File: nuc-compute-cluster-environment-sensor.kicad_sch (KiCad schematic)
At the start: 122 parts, among them J1 USB4105-GF-A, J2 SM04B-SRSS-TB-LF-SN, J3 SM04B-SRSS-TB-LF-SN, U1 FT4232H-56Q, U2 AP7370-33SA-7, U3 STM32G474CET6, U4 MB85RC1MTPNF-G, U5 SHT45, U6 BME280, Y1 ABM3B-12.000MHZ-B2-T, Y2 ECS-_327-12_5-34B-TR, Y3 ABM3B-8.000MHZ-10-1-U-T

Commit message: Reannotate schematic symbols
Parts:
- gave numbers to parts that had none: 1
- renumbered C1 to C51, C2 to C52, C3 to C53, C4 to C54, C5 to C55, C6 to C56, C7 to C57, C8 to C58, C9 to C59, C10 to C60, C11 to C61, C12 to C62, C13 to C63, C14 to C64, C15 to C65, C16 to C66, C17 to C67, C18 to C68, C19 to C69, C20 to C70, C21 to C71, C22 to C72, C23 to C73, C24 to C74, C25 to C75, C26 to C76, C27 to C77, C28 to C78, C29 to C79, C30 to C80, C31 to C81, C32 to C82, C33 to C83, C34 to C84, C35 to C85, C36 to C86, C37 to C87, C38 to C88, C39 to C89, C40 to C90, D1 to D35, D2 to D36, D3 to D37, D4 to D38, D5 to D39, D6 to D40, D7 to D41, D8 to D42, D9 to D43, FB1 to FB13, FB2 to FB14, FB3 to FB15, FB4 to FB16, FB5 to FB17, J1 to J15, J2 to J16, J3 to J17, MP1 to MP17, MP2 to MP18, MP3 to MP19, R1 to R207, R2 to R208, R3 to R209, R4 to R210, R5 to R211, R6 to R212, R7 to R213, R8 to R214, R9 to R215, R10 to R216, R11 to R217, R12 to R218, R13 to R219, R14 to R220, R15 to R221, R16 to R222, R17 to R223, R18 to R224, R19 to R225, R20 to R227, R21 to R228, R22 to R229, R23 to R230, R24 to R231, R25 to R232, R26 to R233, R27 to R234, R28 to R235, R29 to R236, R30 to R237, R31 to R238, R32 to R239, R33 to R240, R34 to R241, R35 to R242, R36 to R243, R37 to R244, R38 to R245, R39 to R246, R40 to R247, TP1 to TP57, TP2 to TP58, TP3 to TP59, TP4 to TP60, TP5 to TP61, TP6 to TP62, TP7 to TP63, TP8 to TP64, TP9 to TP65, U1 to U26, U2 to U27, U3 to U28, U4 to U29, U5 to U30, U6 to U31, Y1 to Y2, Y2 to Y3, Y3 to Y4

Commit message: Set resitsors to standard
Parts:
- renumbered C51 to C50, C52 to C51, C53 to C52, C54 to C53, C55 to C54, C56 to C55, C57 to C56, C58 to C57, C59 to C58, C60 to C59, C61 to C60, C62 to C61, C63 to C62, C64 to C63, C65 to C64, C66 to C65, C67 to C66, C68 to C67, C69 to C68, C70 to C69, C71 to C70, C72 to C71, C73 to C72, C74 to C73, C75 to C74, C76 to C75, C77 to C76, C78 to C77, C79 to C78, C80 to C79, C81 to C80, C82 to C81, C83 to C82, C84 to C83, C85 to C84, C86 to C85, C87 to C86, C88 to C87, C89 to C88, C90 to C89, FB13 to FB12, FB14 to FB13, FB15 to FB14, FB16 to FB15, FB17 to FB16, R207 to R206, R208 to R207, R209 to R208, R210 to R209, R211 to R210, R212 to R211, R213 to R212, R214 to R213, R215 to R214, R216 to R215, R217 to R216, R218 to R217, R219 to R218, R220 to R219, R221 to R220, R222 to R221, R223 to R222, R224 to R223, R225 to R224, R226 to R225, R227 to R226, R228 to R227, R229 to R228, R230 to R229, R231 to R230, R232 to R231, R233 to R232, R234 to R233, R235 to R234, R236 to R235, R237 to R236, R238 to R237, R239 to R238, R240 to R239, R241 to R240, R242 to R241, R243 to R242, R244 to R243, R245 to R244, R246 to R245, R247 to R246

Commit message: Repleace non standard components in connectors and ftdi and power
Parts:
- renumbered C50 to C51, C51 to C52, C52 to C53, C53 to C54, C54 to C55, C55 to C56, C56 to C57, C57 to C58, C58 to C59, C59 to C60, C60 to C61, C61 to C62, C62 to C63, C63 to C64, C64 to C65, C65 to C66, C66 to C67, C67 to C68, C68 to C69, C69 to C70, C70 to C71, C71 to C72, C72 to C73, C73 to C74, C74 to C75, C75 to C76, C76 to C77, C77 to C78, C78 to C79, C79 to C80, C80 to C81, C81 to C82, C82 to C83, C83 to C84, C84 to C85, C85 to C86, C86 to C87, C87 to C88, C88 to C89, C89 to C90, R206 to R222, R207 to R223, R208 to R224, R209 to R225, R210 to R226, R211 to R227, R212 to R228, R213 to R229, R214 to R230, R215 to R231, R216 to R232, R217 to R233, R218 to R234, R219 to R235, R220 to R236, R221 to R237, R222 to R238, R223 to R239, R224 to R240, R225 to R241, R226 to R242, R227 to R243, R228 to R244, R229 to R245, R230 to R246, R231 to R247, R232 to R248, R233 to R249, R234 to R250, R235 to R251, R236 to R252, R237 to R253, R238 to R254, R239 to R255, R240 to R256, R241 to R257, R242 to R258, R243 to R259, R244 to R260, R245 to R261, R246 to R262, U26 to U25, U27 to U26, U28 to U27, U29 to U28, U30 to U29, U31 to U30

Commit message: Standarize debug signal schematic
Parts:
- renumbered R222 to R230, R223 to R231, R224 to R232, R225 to R233, R226 to R234, R227 to R235, R228 to R236, R229 to R237, R230 to R238, R231 to R239, R232 to R240, R233 to R241, R234 to R242, R235 to R243, R236 to R244, R237 to R245, R238 to R246, R239 to R247, R240 to R248, R241 to R249, R242 to R250, R243 to R251, R244 to R252, R245 to R253, R246 to R254, R247 to R255, R248 to R256, R249 to R257, R250 to R258, R251 to R259, R252 to R260, R253 to R261, R254 to R262, R255 to R263, R256 to R264, R257 to R265, R258 to R266, R259 to R267, R260 to R268, R261 to R269, R262 to R270

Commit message: Standarize env sensor schematic
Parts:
- removed LD2: LG_L29K-G2J1-24-Z, antmicro-footprints:LED_0603, symbol antmicroLEDIndicationDiscrete:KP-1608ZGC
- removed R233, R252, R258: R_1M0_0402, antmicro-footprints:0402-res, symbol antmicroResistors0402:R_1M0_0402
- added D?: LED_R_0603_KP-1608EC, antmicro-footprints:LED_0603_1608Metric_R, symbol antmicroLEDIndicationDiscrete:LED_R_0603_KP-1608EC
- added R? (x3): R_1M_0402, antmicro-footprints:R_0402_1005Metric, symbol antmicroResistors0402:R_1M_0402
- BAT1: Author (none) -> Antmicro; License Copyright (c) 2022 Antmicro <www.antmicro.com> [Apache2 lic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 -> Apache-2.0
- C51, C64, C66, C68, C69, C73, C82, C86: footprint antmicro-footprints:0402-cap -> antmicro-footprints:C_0402_1005Metric; Author (none) -> Antmicro; License (none) -> Apache-2.0
- C52, C55, C56, C62, C71, C72: footprint antmicro-footprints:0402-cap -> antmicro-footprints:C_0402_1005Metric; Author (none) -> Antmicro; License (none) -> Apache-2.0; Manufacturer MURATA -> Murata
- C53, C54, C57, C58, C59, C60, C61, C67, C70, C74, C75, C77, C79, C80, C81, C84, C87, C88, C89, C90: footprint antmicro-footprints:0402-cap -> antmicro-footprints:C_0402_1005Metric; Author (none) -> Antmicro; Dielectric (none) -> X5R; License (none) -> Apache-2.0; Voltage (none) -> 50V
- C63, C65: footprint antmicro-footprints:0402-cap -> antmicro-footprints:C_0402_1005Metric; Author (none) -> Antmicro; License (none) -> Apache-2.0; MPN GRM155R61H104KE14D -> GRM155R61A475MEAAD; Manufacturer MURATA -> Murata; Val 100n -> 4u7
- C76, C78: footprint antmicro-footprints:0402-res -> antmicro-footprints:C_0402_1005Metric; Author (none) -> Antmicro; License (none) -> Apache-2.0
- C83, C85: footprint antmicro-footprints:0402-cap -> antmicro-footprints:C_0402_1005Metric; Author (none) -> Antmicro; Dielectric (none) -> C0G; License (none) -> Apache-2.0; MPN MC0402N100D500CT -> GCM1555C1H100GA16D; Manufacturer MULTICOMP -> Murata; Voltage (none) -> 50V
- D35, D36, D37, D38, D41, D43, U26, U29: Author (none) -> Antmicro; License (none) -> Apache-2.0
- R231, R232, R269, R270: footprint antmicro-footprints:0402-res -> antmicro-footprints:R_0402_1005Metric; Author (none) -> Antmicro; License (none) -> Apache-2.0; MPN SFR01MZPJ512 -> CR0402-FX-5101GLF; Manufacturer ROHM Semiconductor -> Bourns; Tolerance (none) -> 1%
- R234, R253, R254, R256, R259, R260: footprint antmicro-footprints:0402-res -> antmicro-footprints:R_0402_1005Metric; Author (none) -> Antmicro; License (none) -> Apache-2.0; Manufacturer BOURNS -> Bourns; Tolerance (none) -> 1%
- R235: footprint antmicro-footprints:0402-res -> antmicro-footprints:R_0402_1005Metric; Author (none) -> Antmicro; License (none) -> Apache-2.0; MPN CRCW040212K0FKEDHP -> CR0402-FX-1202GLF; Manufacturer VISHAY -> Bourns; Tolerance ±1% -> 1%
- R236, R238, R239, R250: footprint antmicro-footprints:0402-res -> antmicro-footprints:R_0402_1005Metric; Author (none) -> Antmicro; License (none) -> Apache-2.0; MPN CRCW0402470RFKED -> CR0402-FX-4700GLF; Manufacturer VISHAY -> Bourns; Tolerance (none) -> 1%
- R237, R240, R241, R242, R243, R244, R245, R246, R247, R248, R255: footprint antmicro-footprints:0402-res -> antmicro-footprints:R_0402_1005Metric; Author (none) -> Antmicro; Current (none) -> 1A; License (none) -> Apache-2.0; Manufacturer PANASONIC -> Panasonic
- R251, R261, R262, R263, R264, R265, R266, R267, R268: footprint antmicro-footprints:0402-res -> antmicro-footprints:R_0402_1005Metric; Author (none) -> Antmicro; License (none) -> Apache-2.0; MPN CRCW0402100KFKEDHP -> CR0402-FX-1003GLF; Manufacturer VISHAY -> Bourns; Tolerance (none) -> 1%
- R257: footprint antmicro-footprints:0402-res -> antmicro-footprints:R_0402_1005Metric; Author (none) -> Antmicro; License (none) -> Apache-2.0; MPN CRCW04021K00FKEDHP -> CR0402-FX-1003GLF; Manufacturer VISHAY -> Bourns; Tolerance (none) -> 1%; Val 1k -> 100k
- U27: Author (none) -> Antmicro; License Copyright (c) 2022 Antmicro <www.antmicro.com> [Apache2 lic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 -> Apache-2.0; Manufacturer ST Microelectronics -> STMicroelectronics
- U28: footprint antmicro-footprints:SOIC-8_W3.9mm -> antmicro-footprints:SOP-8_3.9x5.05mm_P1.27mm; Author (none) -> Antmicro; License (none) -> Apache-2.0; Manufacturer Fujitsu Semiconductor Ltd -> Fujitsu
- U30: footprint antmicro-footprints:Pressure_Sensor_LGA-8_2.5x2.5mm_BME280 -> antmicro-footprints:LGA-8_2.5x2.5mm_BME280; Author (none) -> Antmicro; License (none) -> Apache-2.0; Manufacturer Bosch Sensortec -> Bosch
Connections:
- net 3V3_ENV: now also C51.2, C52.2, C53.2, C57.2, C58.2, C61.2, C72.2, C73.2, C74.1, C87.1, C88.1, C89.1, C90.1, R267.1; no longer C51.1, C52.1, C53.1, C57.1, C58.1, C61.1, C72.1, C73.1, C74.2, C87.2, C88.2, C89.2, C90.2, R267.2
- net FTDI_+1V8: now also C62.2; no longer C62.1
- net GND: now also C51.1, C52.1, C53.1, C54.1, C57.1, C58.1, C61.1, C62.1, C64.2, C66.1, C68.2, C69.1, C70.1, C72.1, C73.1, C74.2, C76.2, C78.2, C81.2, C82.1, C84.2, C86.1, C87.2, C88.2, C89.2, C90.2, R264.2; no longer C51.2, C52.2, C53.2, C54.2, C57.2, C58.2, C61.2, C62.2, C64.1, C66.2, C68.1, C69.2, C70.2, C72.2, C73.2, C74.1, C76.1, C78.1, C81.1, C82.2, C84.1, C86.2, C87.1, C88.1, C89.1, C90.1, R264.1
- net GNDREF: now also C54.2; no longer C54.1
- net LD2: now also D?.1
- net VBUS: now also C66.2; no longer C66.1
- net at U25.4 (OSCO), Y2.1: now also C68.1, R?.2; no longer C68.2
- net at U25.3 (OSCI), Y2.3: now also C64.1, R?.1; no longer C64.2
- net at FB15.1, LD1.1, U26.3 (VIN): now also C69.2, C70.2; no longer C69.1, C70.1
- net at C83.2, U27.6 (PF1-OSC_OUT), Y4.1: now also R?.1
- net at C85.2, U27.5 (PF0-OSC_IN), Y4.3: now also R?.2
- net at R268.2, U30.5 (SDO): now also R267.2; no longer R267.1
- net at R259.1, R263.1, TP61.1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: now also R264.1; no longer R264.2
- net at U27.1 (VBAT): now also BAT1.P1, BAT1.P2; no longer BAT1.P
- net at FB16.1, U27.21 (VDDA): now also C81.1, C82.2; no longer C81.2, C82.1
- net at U27.3 (PC14-OSC32_IN), Y3.1: now also C76.1, R?.1; no longer C76.2
- net at U27.4 (PC15-OSC32_OUT), Y3.2: now also C78.1, R?.2; no longer C78.2
- net at R250.2: now also D?.2
- net FTDI_SDA_IN: no longer names the net of R243.1, U25.24 (BDBUS2)
- net FTDI_SDA_OUT: no longer names the net of R242.1, U25.23 (BDBUS1)
- new net: C84.1, C86.2, U27.20 (VREF+)
- no-connect marks 46 -> 45
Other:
- moved on the sheet: C51, C52, C53, C54, C55, C56, C57, C58, C59, C60, C61, C62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

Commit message: Cleanup project
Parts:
- gave numbers to parts that had none: 4
- renumbered D40 to D41, D41 to D42, D42 to D43, D43 to D44, R240 to R238, R241 to R239, R242 to R240, R243 to R241, R244 to R242, R245 to R243, R246 to R244, R247 to R245, R248 to R246, R238 to R247, R239 to R248, R251 to R252, R255 to R253, R256 to R254, R253 to R255, R254 to R256, R257 to R258

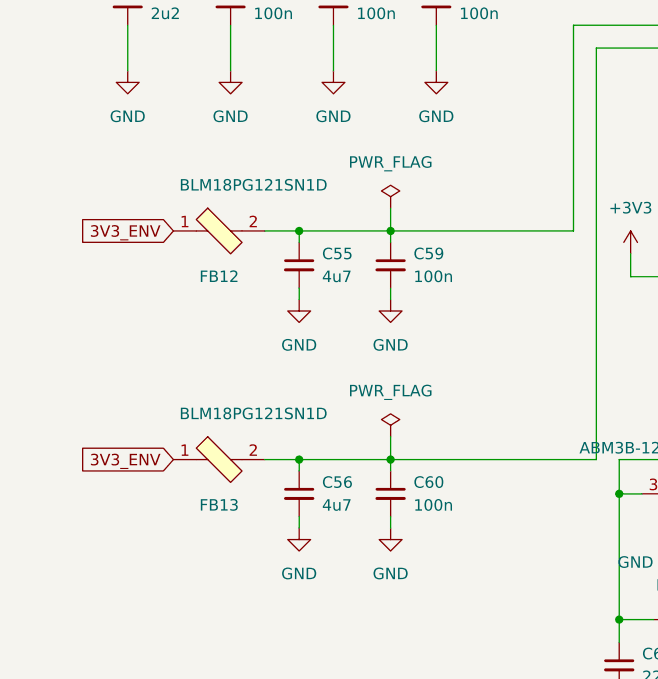
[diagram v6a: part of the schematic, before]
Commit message: Standarize missing components
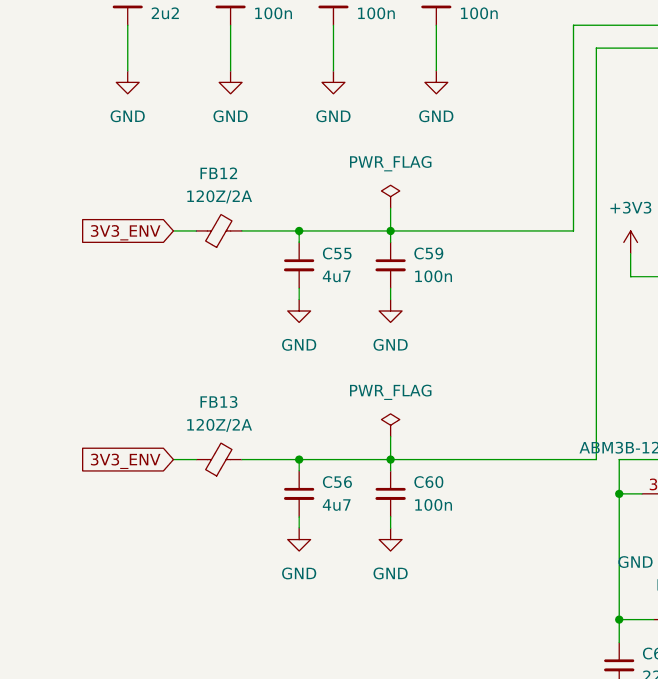
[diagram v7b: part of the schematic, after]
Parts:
- removed FB12, FB13: BLM18PG121SN1D, antmicro-footprints:0603-res, symbol antmicroFerriteBeadsandChips:BLM18PG121SN1D
- added FB12, FB13: FB_120Z_2A_Murata-BLM18PG_0603, antmicro-footprints:FB_0603_1608Metric, symbol antmicroFerriteBeadsandChips:FB_120Z_2A_Murata-BLM18PG_0603
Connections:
- net 3V3_ENV: now also FB12.1, FB13.1
- net FTDI_VPHY: now also FB12.2
- net FTDI_VPLL: now also FB13.2

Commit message: 2nd batch of standardization of schematic
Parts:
- removed D39, D41, D43: TPD2E009, antmicro-footprints:SOT-723, symbol antmicroTVSDiodes:TPD2E009
- removed FB14, FB15, FB16: BLM18PG121SN1D, antmicro-footprints:0603-res, symbol antmicroFerriteBeadsandChips:BLM18PG121SN1D
- removed J16: SM04B-SRSS-TB-LF-SN, antmicro-footprints:SM04B-SRSS-TB-LF-SN, symbol antmicroRectangularConnectorsHeadersMalePins:SM04B-SRSS-TB-LF-SN
- removed TP62, TP63, TP64, TP65: TP_SMD1MM, antmicro-footprints:Testpoint_smd_1mm, symbol antmicroTestPoints:TP_SMD1MM
- removed Y4: ABM3B-8.000MHZ-10-1-U-T, antmicro-footprints:ABM3B, symbol antmicroCrystals:ABM3B-8.000MHZ-10-1-U-T
- added D? (x3): TPD2E009_SOT-9X3, antmicro-footprints:SOT-723, symbol antmicroTVSDiodes:TPD2E009_SOT-9X3
- added FB? (x3): FB_120Z_2A_Murata-BLM18PG_0603, antmicro-footprints:FB_0603_1608Metric, symbol antmicroFerriteBeadsandChips:FB_120Z_2A_Murata-BLM18PG_0603
- added J?: SM04B-SRSS-TB-LF-SN, antmicro-footprints:SM04B-SRSS-TB-LF-SN, symbol antmicroGenericPinHeaders:SM04B-SRSS-TB-LF-SN
- added TP? (x4): TP_1mm_SMD, antmicro-footprints:TP_SMD_1mm, symbol antmicroTestPoints:TP_1mm_SMD
- added Y?: Resonator_8MHz_ABM3B, antmicro-footprints:ABM3B, symbol antmicroResonators:Resonator_8MHz_ABM3B
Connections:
- net 3V3_ENV: now also FB?.1, J?.2, TP?.1
- net GND: now also D?.3, D?.3, D?.3, FB?.2, J?.1, TP?.1, Y?.2 (SH), Y?.4 (SH)
- net GNDREF: now also FB?.1
- net I2C_1_SCL: now also D?.1, D?.1, J?.4, TP?.1
- net I2C_1_SDA: now also D?.2, D?.2, J?.3, TP?.1
- net USB_D_N: now also D?.2
- net USB_D_P: now also D?.1
- net VBUS: now also FB?.1
- net at C69.2, C70.2, LD1.1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: now also FB?.2
- net at C83.2, R257.1, U27.6 (PF1-OSC_OUT): now also Y?.1
- net at C85.2, R257.2, U27.5 (PF0-OSC_IN): now also Y?.3
- net at C81.1, C82.2, U27.21 (VDDA): now also FB?.2
- new net: J?.S1 (SH), J?.S2 (SH)
